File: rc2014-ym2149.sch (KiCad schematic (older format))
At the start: 7 parts

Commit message: updated schematic
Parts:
- added U?: 74HCT74, symbol 74LS74
- added U? (x2): 74HCT32, symbol 74LS32
- R?: value R -> 10K
- U?: value 74LS138 -> 74HCT138
- U?: value 74LS245 -> 74HCT245
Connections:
- net labels added: /IORQ, /RD, /WR
- net labels removed: IORQ, RD, WR
- wire segments 93 -> 120
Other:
- note added: "A14 & A15 high = control = y7 low\nA14 low and A15 high = data = y5 low"
- moved on the sheet: P?
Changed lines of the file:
@@
 P 3700 2200
 F 0 "U?" H 3800 2700 50  0000 C CNN
-F 1 "74LS138" H 3850 1651 50  0000 C CNN
+F 1 "74HCT138" H 3850 1651 50  0000 C CNN
 F 2 "" H 3700 2200 50  0000 C CNN
 F 3 "" H 3700 2200 50  0000 C CNN
@@
 P 3700 3750
 F 0 "U?" H 3800 4325 50  0000 L BNN
-F 1 "74LS245" H 3750 3175 50  0000 L TNN
+F 1 "74HCT245" H 3750 3175 50  0000 L TNN
 F 2 "" H 3700 3750 50  0000 C CNN
 F 3 "" H 3700 3750 50  0000 C CNN
@@
 L CONN_02X08 P?
 U 1 1 58979497
-P 4900 2300
-F 0 "P?" H 4900 2750 50  0000 C CNN
-F 1 "CONN_02X08" V 4900 2300 50  0000 C CNN
-F 2 "" H 4900 1100 50  0000 C CNN
-F 3 "" H 4900 1100 50  0000 C CNN
-	1    4900 2300
+P 4700 1150
+F 0 "P?" H 4700 1600 50  0000 C CNN
+F 1 "CONN_02X08" V 4700 1150 50  0000 C CNN
+F 2 "" H 4700 -50 50  0000 C CNN
+F 3 "" H 4700 -50 50  0000 C CNN
+	1    4700 1150
 	1    0    0    -1
 $EndComp
@@
 MREQ
 Text Label 1800 4100 0    60   ~ 0
-WR
+/WR
 Text Label 1800 4200 0    60   ~ 0
-RD
+/RD
 Text Label 1800 4300 0    60   ~ 0
-IORQ
+/IORQ
 $Comp
 L GND #PWR?
@@
 P 7150 1750
 F 0 "R?" V 7230 1750 50  0000 C CNN
-F 1 "R" V 7150 1750 50  0000 C CNN
+F 1 "10K" V 7150 1750 50  0000 C CNN
 F 2 "" V 7080 1750 50  0000 C CNN
 F 3 "" H 7150 1750 50  0000 C CNN
@@
 	1750 2700 2000 2700
 Wire Wire Line
-	1750 4100 2000 4100
+	1750 4100 2150 4100
 Wire Wire Line
 	1750 2800 2000 2800
@@
 	1750 3700 2000 3700
 Wire Wire Line
-	1750 3800 2000 3800
+	1750 3800 2700 3800
 Wire Wire Line
 	1750 3900 2000 3900
@@
 	1750 5700 2000 5700
 Wire Wire Line
-	1750 4200 2000 4200
+	1750 4200 2500 4200
 Wire Wire Line
 	5850 2150 5700 2150
@@
 	6550 3150 6700 3150
 Wire Wire Line
-	6550 3250 7000 3250
+	6550 3250 7700 3250
 Wire Wire Line
 	6550 3350 7400 3350
 Wire Wire Line
-	6550 3450 7000 3450
-Wire Wire Line
-	6550 3550 6700 3550
-Wire Wire Line
-	6550 3650 6700 3650
-Wire Wire Line
-	6550 3750 6700 3750
+	6550 3450 7600 3450
+Wire Wire Line
+	6550 3550 7300 3550
+Wire Wire Line
+	6550 3650 7100 3650
+Wire Wire Line
+	6550 3750 7100 3750
 Wire Wire Line
 	6550 3850 6700 3850
@@
 Wire Wire Line
 	2500 2450 3100 2450
+$Comp
+L 74LS74 U?
+U 1 1 58ACAA95
+P 5700 5300
+F 0 "U?" H 5850 5600 50  0000 C CNN
+F 1 "74HCT74" H 6000 5005 50  0000 C CNN
+F 2 "" H 5700 5300 50  0000 C CNN
+F 3 "" H 5700 5300 50  0000 C CNN
+	1    5700 5300
+	1    0    0    -1
+$EndComp
+Wire Wire Line
+	3100 2050 3000 2050
+$Comp
+L VCC #PWR?
+U 1 1 58ACB16A
+P 3000 2050
+F 0 "#PWR?" H 3000 1900 50  0001 C CNN
+F 1 "VCC" H 3000 2200 50  0000 C CNN
+F 2 "" H 3000 2050 50  0000 C CNN
+F 3 "" H 3000 2050 50  0000 C CNN
+	1    3000 2050
+	1    0    0    -1
+$EndComp
+Text Notes 1900 1450 0    60   ~ 0
+A14 & A15 high = control = y7 low\nA14 low and A15 high = data = y5 low
+$Comp
+L 74LS32 U?
+U 1 1 58ACB2E3
+P 3450 4850
+F 0 "U?" H 3450 4900 50  0000 C CNN
+F 1 "74HCT32" H 3450 4800 50  0000 C CNN
+F 2 "" H 3450 4850 50  0000 C CNN
+F 3 "" H 3450 4850 50  0000 C CNN
+	1    3450 4850
+	1    0    0    -1
+$EndComp
+$Comp
+L 74LS32 U?
+U 2 1 58ACB332
+P 3450 5450
+F 0 "U?" H 3450 5500 50  0000 C CNN
+F 1 "74HCT32" H 3450 5400 50  0000 C CNN
+F 2 "" H 3450 5450 50  0000 C CNN
+F 3 "" H 3450 5450 50  0000 C CNN
+	2    3450 5450
+	1    0    0    -1
+$EndComp
+Wire Wire Line
+	2500 4200 2500 4750
+Wire Wire Line
+	2500 4750 2850 4750
+Wire Wire Line
+	2300 4300 2300 5550
+Wire Wire Line
+	2300 4950 2850 4950
+Connection ~ 2300 4300
+Wire Wire Line
+	2150 4100 2150 5350
+Wire Wire Line
+	2150 5350 2850 5350
+Wire Wire Line
+	2300 5550 2850 5550
+Connection ~ 2300 4950
+Wire Wire Line
+	4050 4850 4400 4850
+Wire Wire Line
+	4400 4850 4400 4350
+Wire Wire Line
+	4400 4350 7700 4350
+Wire Wire Line
+	7700 4350 7700 3250
+Wire Wire Line
+	4050 5450 4500 5450
+Wire Wire Line
+	4500 5450 4500 4450
+Wire Wire Line
+	4500 4450 7600 4450
+Wire Wire Line
+	7600 4450 7600 3450
+Wire Wire Line
+	6300 5500 6650 5500
+Wire Wire Line
+	6650 5500 6650 4600
+Wire Wire Line
+	6650 4600 4850 4600
+Wire Wire Line
+	4850 4600 4850 5100
+Wire Wire Line
+	4850 5100 5100 5100
+Wire Wire Line
+	6300 5100 7650 5100
+Wire Wire Line
+	7650 5100 7650 3950
+$Comp
+L VCC #PWR?
+U 1 1 58B1CE4E
+P 5700 4750
+F 0 "#PWR?" H 5700 4600 50  0001 C CNN
+F 1 "VCC" H 5700 4900 50  0000 C CNN
+F 2 "" H 5700 4750 50  0000 C CNN
+F 3 "" H 5700 4750 50  0000 C CNN
+	1    5700 4750
+	1    0    0    -1
+$EndComp
+$Comp
+L VCC #PWR?
+U 1 1 58B1CE76
+P 5700 5850
+F 0 "#PWR?" H 5700 5700 50  0001 C CNN
+F 1 "VCC" H 5700 6000 50  0000 C CNN
+F 2 "" H 5700 5850 50  0000 C CNN
+F 3 "" H 5700 5850 50  0000 C CNN
+	1    5700 5850
+	-1   0    0    1
+$EndComp
+Wire Wire Line
+	4600 5300 5100 5300
+Wire Wire Line
+	2700 3800 2700 4550
+Wire Wire Line
+	2700 4550 4600 4550
+Wire Wire Line
+	4600 4550 4600 5300
+$Comp
+L GND #PWR?
+U 1 1 58B20AA2
+P 7300 3550
+F 0 "#PWR?" H 7300 3300 50  0001 C CNN
+F 1 "GND" H 7300 3400 50  0000 C CNN
+F 2 "" H 7300 3550 50  0000 C CNN
+F 3 "" H 7300 3550 50  0000 C CNN
+	1    7300 3550
+	1    0    0    -1
+$EndComp
+$Comp
+L GND #PWR?
+U 1 1 58B210E6
+P 7100 3750
+F 0 "#PWR?" H 7100 3500 50  0001 C CNN
+F 1 "GND" H 7100 3600 50  0000 C CNN
+F 2 "" H 7100 3750 50  0000 C CNN
+F 3 "" H 7100 3750 50  0000 C CNN
+	1    7100 3750
+	1    0    0    -1
+$EndComp
+$Comp
+L VCC #PWR?
+U 1 1 58B2110E
+P 7100 3650
+F 0 "#PWR?" H 7100 3500 50  0001 C CNN
+F 1 "VCC" H 7100 3800 50  0000 C CNN
+F 2 "" H 7100 3650 50  0000 C CNN
+F 3 "" H 7100 3650 50  0000 C CNN
+	1    7100 3650
+	1    0    0    -1
+$EndComp
 $EndSCHEMATC

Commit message: experiment with playing yms
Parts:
- removed U? (x2): 74HCT32, symbol 74LS32
- added C?: 0.1uF, symbol C
- added U? (x2): 74HCT00, symbol 74HCT00
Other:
- note removed: "A14 & A15 high = control = y7 low\nA14 low and A15 high = data = y5 low"
- moved on the sheet: J?, P?

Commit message: start laying out pcb
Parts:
- removed R?: 10K, symbol R
- removed U?: 74HCT245, symbol 74LS245
- added C2, C3: 470uF, Capacitors_THT:CP_Radial_D5.0mm_P2.50mm, symbol CP
- added JP1: 1/2 CLK, Pin_Headers:Pin_Header_Straight_1x02_Pitch2.54mm, symbol Jumper_NC_Small
- added JP2: 1/4 CLK, Pin_Headers:Pin_Header_Straight_1x02_Pitch2.54mm, symbol Jumper_NO_Small
- added JP3: YM 1/2 CLK, Pin_Headers:Pin_Header_Straight_1x02_Pitch2.54mm, symbol Jumper
- added P4: IO Out, Pin_Headers:Pin_Header_Angled_2x09_Pitch2.54mm, symbol CONN_02X09
- added R1, R2, R3: 470R, Resistors_THT:R_Axial_DIN0207_L6.3mm_D2.5mm_P7.62mm_Horizontal, symbol R_Small
- added R4, R5: 1K, Resistors_THT:R_Axial_DIN0207_L6.3mm_D2.5mm_P7.62mm_Horizontal, symbol R_Small
- added R6, R7: 1K6, Resistors_THT:R_Axial_DIN0207_L6.3mm_D2.5mm_P7.62mm_Horizontal, symbol R_Small
- added unit 2 of U4
- C1: renamed from C?; footprint (none) -> Capacitors_THT:C_Disc_D3.8mm_W2.6mm_P2.50mm
- J1: renamed from J?; footprint (none) -> Pin_Headers:Pin_Header_Straight_2x03_Pitch2.54mm
- P1: renamed from P?; footprint (none) -> Pin_Headers:Pin_Header_Angled_1x40_Pitch2.54mm
- P2: renamed from P?; footprint (none) -> Pin_Headers:Pin_Header_Straight_2x08_Pitch2.54mm
- P3: renamed from P?; value DIL40 -> AY-3-8190/YM2149F; footprint (none) -> Housings_DIP:DIP-40_W15.24mm_Socket
- U1: renamed from U?; footprint (none) -> Housings_DIP:DIP-16_W7.62mm_Socket
- U3, U4: renamed from U?; footprint (none) -> Housings_DIP:DIP-14_W7.62mm_Socket
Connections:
- net labels removed: DA0, DA1, DA2, DA3, DA4, DA5, DA6, DA7
- wire segments 120 -> 167
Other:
- moved on the sheet: C1, J1, P2, U1

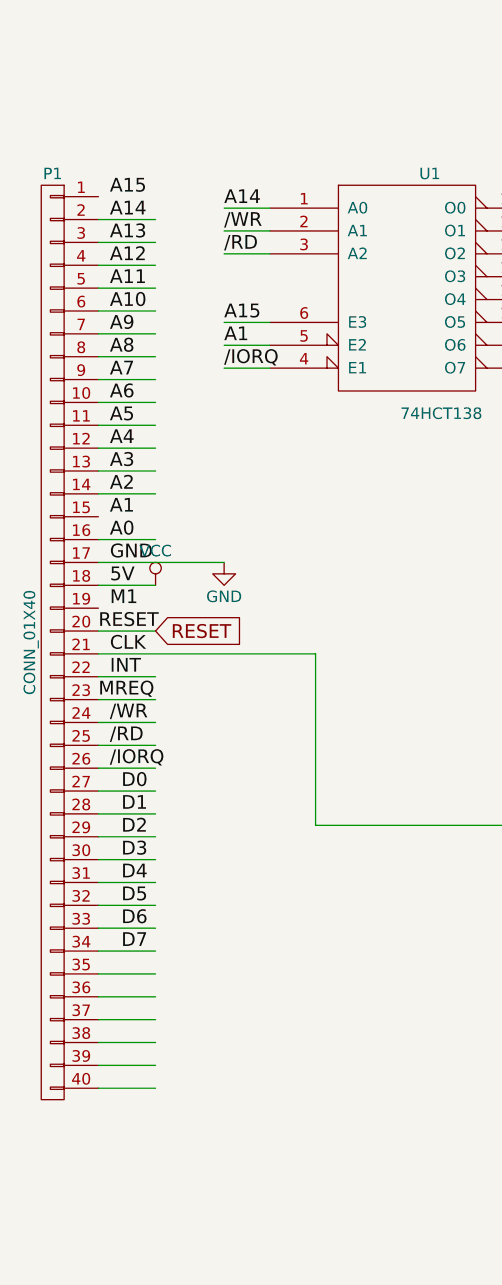
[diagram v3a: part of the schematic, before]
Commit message: make pcb more rc2014 like
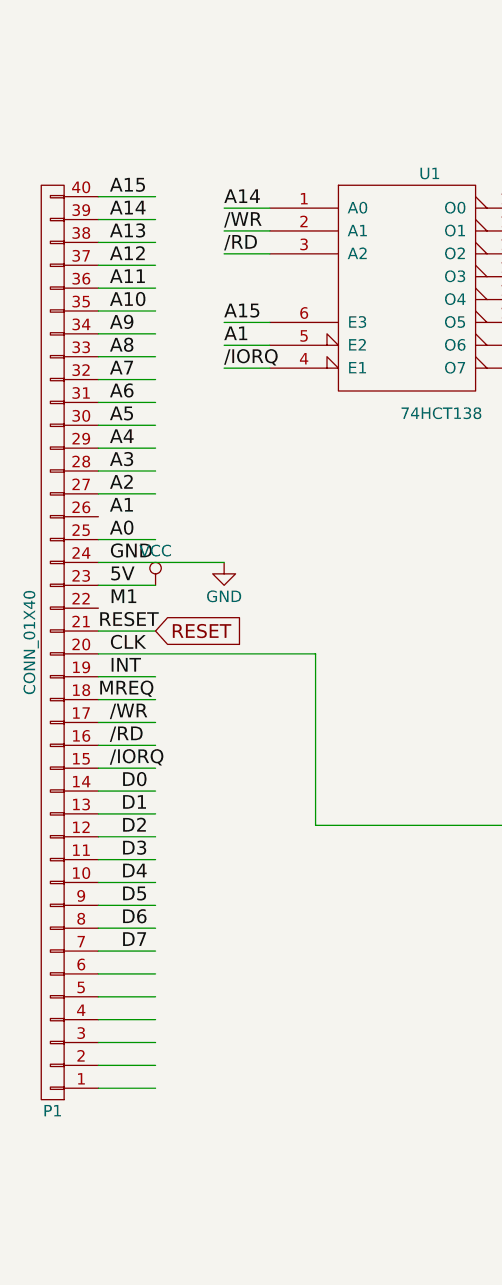
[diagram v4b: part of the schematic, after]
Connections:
- wire segments 167 -> 168
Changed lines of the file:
@@
 F 3 "" H 1550 3750 50  0000 C CNN
 	1    1550 3750
-	-1   0    0    -1
+	-1   0    0    1
 $EndComp
 $Comp
@@
 Text Label 2300 2350 0    60   ~ 0
 A15
+Wire Wire Line
+	1750 1800 2000 1800
 $EndSCHEMATC

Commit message: more work on pcb
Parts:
- added C4, C5, C6: C, Capacitors_THT:C_Disc_D3.8mm_W2.6mm_P2.50mm, symbol C
- P1: value CONN_01X40 -> CONN_01X39; footprint Pin_Headers:Pin_Header_Angled_1x40_Pitch2.54mm -> Pin_Headers:Pin_Header_Angled_1x39_Pitch2.54mm; symbol CONN_01X40 -> CONN_01X39
- P4: footprint Pin_Headers:Pin_Header_Angled_2x09_Pitch2.54mm -> Pin_Headers:Pin_Header_Straight_2x09_Pitch2.54mm
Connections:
- wire segments 168 -> 162
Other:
- note added: "NAND"
- moved on the sheet: P2, U1, U3A, U3B

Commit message: 1st attempt at pcb layout complete
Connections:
- net labels added: /YM_A9, YM_A8
- net labels removed: /A9, RESET
- wire segments 162 -> 164
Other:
- note removed: "NAND"
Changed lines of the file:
@@
 Text Label 1150 3600 0    60   ~ 0
 M1
-Text Label 1100 3700 0    60   ~ 0
-RESET
+Text Label 1150 3700 0    60   ~ 0
+/RESET
 Text Label 1150 3800 0    60   ~ 0
 CLK
 Text Label 1150 3900 0    60   ~ 0
 INT
-Text Label 1100 4000 0    60   ~ 0
+Text Label 1150 4000 0    60   ~ 0
 MREQ
 Text Label 1150 4100 0    60   ~ 0
@@
 Text Label 7000 3450 0    60   ~ 0
 BDIR
-Text Label 6900 3550 0    60   ~ 0
+Text Label 7000 3550 0    60   ~ 0
 /SEL
 Text Label 7000 3650 0    60   ~ 0
-A8
-Text Label 6950 3750 0    60   ~ 0
-/A9
-Text Label 6900 3850 0    60   ~ 0
+YM_A8
+Text Label 7000 3750 0    60   ~ 0
+/YM_A9
+Text Label 7000 3850 0    60   ~ 0
 /RESET
-Text Label 6900 3950 0    60   ~ 0
+Text Label 7000 3950 0    60   ~ 0
 CLOCK
-Text Label 6900 4050 0    60   ~ 0
+Text Label 7000 4050 0    60   ~ 0
 IOA0
 $Comp
@@
 	1    0    0    -1
 $EndComp
-Text GLabel 1350 3700 2    60   Input ~ 0
-RESET
-Text GLabel 7100 3850 2    60   Input ~ 0
-RESET
 $Comp
 L JACK_TRS_6PINS J1
@@
 Wire Wire Line
 	7200 1600 7950 1600
-Connection ~ 7750 1600
 $Comp
 L GND #PWR016
@@
 Wire Wire Line
 	7200 1850 7200 1600
-Connection ~ 7450 1600
 Wire Wire Line
 	8750 600  8750 1200
@@
 	1    0    0    -1
 $EndComp
-Text Notes 4450 1800 0    60   ~ 0
-NAND
 Wire Wire Line
 	5200 2650 5400 2650
@@
 Wire Wire Line
 	6950 3450 7150 3450
+Wire Wire Line
+	1100 3200 1350 3200
+Wire Wire Line
+	1100 3600 1350 3600
 $EndSCHEMATC

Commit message: PCB relayout
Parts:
- J1: footprint Pin_Headers:Pin_Header_Straight_2x03_Pitch2.54mm -> rc2014:cliff_fcr1295_socket
- P1: value CONN_01X39 -> CONN_01X34; footprint Pin_Headers:Pin_Header_Angled_1x39_Pitch2.54mm -> Pin_Headers:Pin_Header_Angled_1x34_Pitch2.54mm; symbol CONN_01X39 -> CONN_01X34
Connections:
- wire segments 164 -> 159
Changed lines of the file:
@@
 $EndDescr
 $Comp
-L CONN_01X39 P1
+L CONN_01X34 P1
 U 1 1 58978FEA
-P 900 3700
-F 0 "P1" H 900 5750 50  0000 C CNN
-F 1 "CONN_01X39" V 1000 3700 50  0000 C CNN
-F 2 "Pin_Headers:Pin_Header_Angled_1x39_Pitch2.54mm" H 900 3700 50  0001 C CNN
-F 3 "" H 900 3700 50  0000 C CNN
-	1    900  3700
+P 900 3450
+F 0 "P1" H 900 5500 50  0000 C CNN
+F 1 "CONN_01X34" V 1000 3450 50  0000 C CNN
+F 2 "Pin_Headers:Pin_Header_Angled_1x34_Pitch2.54mm" H 900 3450 50  0001 C CNN
+F 3 "" H 900 3450 50  0000 C CNN
+	1    900  3450
 	-1   0    0    1
 $EndComp
@@
 F 0 "J1" H 10150 1400 50  0000 C CNN
 F 1 "JACK_TRS_6PINS" H 10100 700 50  0000 C CNN
-F 2 "Pin_Headers:Pin_Header_Straight_2x03_Pitch2.54mm" H 10250 850 50  0001 C CNN
+F 2 "rc2014:cliff_fcr1295_socket" H 10250 850 50  0001 C CNN
 F 3 "" H 10250 850 50  0000 C CNN
 	1    10150 1000
@@
 	1100 5100 1350 5100
 Wire Wire Line
-	1100 5200 1350 5200
-Wire Wire Line
-	1100 5300 1350 5300
-Wire Wire Line
-	1100 5400 1350 5400
-Wire Wire Line
-	1100 5500 1350 5500
-Wire Wire Line
-	1100 5600 1350 5600
-Wire Wire Line
 	6250 2150 6100 2150

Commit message: Update pcb again
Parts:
- removed JP1: 1/2 CLK, Pin_Headers:Pin_Header_Straight_1x02_Pitch2.54mm, symbol Jumper_NC_Small
- removed JP2: 1/4 CLK, Pin_Headers:Pin_Header_Straight_1x02_Pitch2.54mm, symbol Jumper_NO_Small
- added JP1: Jumper_Dual, Pin_Headers:Pin_Header_Straight_1x03_Pitch2.54mm, symbol Jumper_Dual
- P1: value CONN_01X34 -> CONN_01X35; footprint Pin_Headers:Pin_Header_Angled_1x34_Pitch2.54mm -> Pin_Headers:Pin_Header_Angled_1x35_Pitch2.54mm; symbol CONN_01X34 -> CONN_01X35
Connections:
- wire segments 159 -> 166
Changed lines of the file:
@@
 LIBS:contrib
 LIBS:valves
+LIBS:jumper_dual
 LIBS:rc2014-ym2149-cache
 EELAYER 25 0
@@
 $EndDescr
 $Comp
-L CONN_01X34 P1
+L CONN_01X35 P1
 U 1 1 58978FEA
-P 900 3450
-F 0 "P1" H 900 5500 50  0000 C CNN
-F 1 "CONN_01X34" V 1000 3450 50  0000 C CNN
-F 2 "Pin_Headers:Pin_Header_Angled_1x34_Pitch2.54mm" H 900 3450 50  0001 C CNN
-F 3 "" H 900 3450 50  0000 C CNN
-	1    900  3450
+P 900 3500
+F 0 "P1" H 900 5550 50  0000 C CNN
+F 1 "CONN_01X35" V 1000 3500 50  0000 C CNN
+F 2 "Pin_Headers:Pin_Header_Angled_1x35_Pitch2.54mm" H 900 3500 50  0001 C CNN
+F 3 "" H 900 3500 50  0000 C CNN
+	1    900  3500
 	-1   0    0    1
 $EndComp
@@
 	1    0    0    -1
 $EndComp
-$Comp
-L Jumper_NC_Small JP1
-U 1 1 58BC6A81
-P 7500 5100
-F 0 "JP1" H 7500 5180 50  0000 C CNN
-F 1 "1/2 CLK" H 7510 5040 50  0000 C CNN
-F 2 "Pin_Headers:Pin_Header_Straight_1x02_Pitch2.54mm" H 7500 5100 50  0001 C CNN
-F 3 "" H 7500 5100 50  0000 C CNN
-	1    7500 5100
-	1    0    0    -1
-$EndComp
-$Comp
-L Jumper_NO_Small JP2
-U 1 1 58BC6ADE
-P 7500 5350
-F 0 "JP2" H 7500 5430 50  0000 C CNN
-F 1 "1/4 CLK" H 7510 5290 50  0000 C CNN
-F 2 "Pin_Headers:Pin_Header_Straight_1x02_Pitch2.54mm" H 7500 5350 50  0001 C CNN
-F 3 "" H 7500 5350 50  0000 C CNN
-	1    7500 5350
-	1    0    0    -1
-$EndComp
 Entry Wire Line
 	6000 2750 6100 2650
@@
 	4850 5100 5100 5100
 Wire Wire Line
-	8050 3950 8050 5350
+	8050 3950 8050 5650
 Wire Wire Line
 	4600 5300 5100 5300
@@
 Wire Wire Line
 	6300 6650 6900 6650
-Connection ~ 8050 5100
-Wire Wire Line
-	6300 5100 7400 5100
-Wire Wire Line
-	7600 5100 8050 5100
-Wire Wire Line
-	8050 5350 7600 5350
+Wire Wire Line
+	6300 5100 7700 5100
 Wire Wire Line
 	6900 6650 6900 5350
-Wire Wire Line
-	6900 5350 7400 5350
 Wire Bus Line
 	6000 2750 6000 4200
@@
 	7350 4050 7350 4100
 Wire Wire Line
-	9750 1000 9150 1000
-Wire Wire Line
-	9750 800  9150 800
-Wire Wire Line
-	9750 1200 9150 1200
+	9150 1000 9750 1000
+Wire Wire Line
+	9150 800  9750 800
+Wire Wire Line
+	9150 1200 9750 1200
 Wire Wire Line
 	9150 1200 9150 1300
@@
 Wire Wire Line
 	1100 3600 1350 3600
+Wire Wire Line
+	9750 1100 9600 1100
+Wire Wire Line
+	9600 1100 9600 1000
+Connection ~ 9600 1000
+Wire Wire Line
+	9750 1300 9600 1300
+Wire Wire Line
+	9600 1300 9600 1200
+Connection ~ 9600 1200
+Wire Wire Line
+	9750 900  9600 900
+Wire Wire Line
+	9600 900  9600 800
+Connection ~ 9600 800
+Wire Wire Line
+	8050 5650 7450 5650
+Wire Wire Line
+	7450 5650 7450 5450
+Wire Wire Line
+	6900 5350 7200 5350
+Wire Wire Line
+	7700 5100 7700 5350
+$Comp
+L Jumper_Dual JP1
+U 1 1 58D043AC
+P 7450 5350
+F 0 "JP1" H 7500 5250 50  0000 L CNN
+F 1 "Jumper_Dual" H 7450 5450 50  0000 C BNN
+F 2 "Pin_Headers:Pin_Header_Straight_1x03_Pitch2.54mm" H 7450 5350 50  0001 C CNN
+F 3 "" H 7450 5350 50  0001 C CNN
+	1    7450 5350
+	1    0    0    -1
+$EndComp
 $EndSCHEMATC
